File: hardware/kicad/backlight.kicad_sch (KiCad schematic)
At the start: 6 parts, among them J701 Retroilluminazione display, J702 USB del Pico (TP2/TP3), J703 USB del Pi Zero 2 W, U701 TPS61169 (Adafruit 6354)

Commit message: Translate code, hardware and docs to English; bilingual dashboard
- tdm-logic i18n module: every dashboard text in English and Italian,
  chosen by `[display] language` in the profile (English by default, the
  TDM 850 profile keeps Italian); number formatting per language
- Slint fixed labels moved to a `Labels` global filled from the same table;
  `tdm-dash --language en|it`; reference screens regenerated in English with
  Italian check screens
- tdmctl, tdm-dash CLI, simulator scenarios, calibration errors and tools
  print English
- KiCad sheets, WireViz harnesses, perfboard plan and CAD comments in
  English, exports regenerated with the new names
- manual, research, ADRs and READMEs translated; files renamed (docs/manual,
  docs/research, English chapter and ADR names); status markers are now
  [VERIFIED] / [TO VERIFY] / [HYPOTHESIS]

Co-Authored-By: Claude Opus 5.5 <noreply@anthropic.com>
Claude-Session: https://claude.ai/code/session_01G9D4Wshjz9MkaThp4wsrGP
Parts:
- J701: value Retroilluminazione display -> Display backlight
- J702: value USB del Pico (TP2/TP3) -> Pico USB (TP2/TP3)
- J703: value USB del Pi Zero 2 W -> Pi Zero 2 W USB
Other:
- note added: "1 VBUS (not connected) · 2 D− · 3 D+ · 4 GND Short twisted pair, ferrite on the cable."
- note added: "Backlight and USB to the Pi"
- note added: "The Pico drives the TPS61169 with 25 kHz PWM (GP15). 100 kΩ to ground: until the firmware runs, the backlight stays off (fail-dark). Newhaven display: LED 180 mA at 9.3 V. Module and display pins [TO VERIFY]. USB: only D+, D− and ground. VBUS not connected: the Pico is supplied from VSYS."
- note added: "The display connects to the Pi through the Adafruit DPI Kippah (40-pin FFC connector, off this board)."
- note removed: "1 VBUS (non collegato) · 2 D− · 3 D+ · 4 GND Doppino intrecciato corto, ferrite sul cavo."
- note removed: "Il Pico comanda il TPS61169 in PWM a 25 kHz (GP15). 100 kΩ verso massa: finché il firmware non parte la retroilluminazione resta spenta (fail-dark). Display Newhaven: LED 180 mA a 9,3 V. Pin del modulo e del display [DA VERIFICARE]. USB: solo D+, D− e massa. VBUS non collegato: il Pico si alimenta da VSYS."
- note removed: "Il display si collega al Pi con l'Adafruit DPI Kippah (connettore FFC 40 poli, fuori da questa scheda)."
- note removed: "Retroilluminazione e USB verso il Pi"
- title: Retroilluminazione e collegamento al Pi -> Backlight and link to the Pi
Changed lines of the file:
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@@
 	(paper "A4")
 	(title_block
-		(title "Retroilluminazione e collegamento al Pi")
+		(title "Backlight and link to the Pi")
 		(date "2026-10-21")
 		(rev "0.1")
 		(company "tdm-dash · CERN-OHL-P-2.0")
-		(comment 1 "Foglio 7 di 8")
-		(comment 2 "Generato da hardware/kicad/generate.py: non modificare a mano")
+		(comment 1 "Sheet 7 of 8")
+		(comment 2 "Generated by hardware/kicad/generate.py: do not edit by hand")
 	)
 	(symbol
@@
 			)
 		)
-		(property "Value" "Retroilluminazione display"
+		(property "Value" "Display backlight"
 			(at 155.194 68.58 0)
 			(effects
@@
 			)
 		)
-		(property "Value" "USB del Pico (TP2/TP3)"
+		(property "Value" "Pico USB (TP2/TP3)"
 			(at 50.8 134.62 0)
 			(effects
@@
 			)
 		)
-		(property "Value" "USB del Pi Zero 2 W"
+		(property "Value" "Pi Zero 2 W USB"
 			(at 139.7 134.62 0)
 			(effects
@@
 		)
 	)
-	(text "Retroilluminazione e USB verso il Pi"
+	(text "Backlight and USB to the Pi"
 		(exclude_from_sim no)
 		(at 10.16 12.7 0)
@@
 		)
 	)
-	(text "Il Pico comanda il TPS61169 in PWM a 25 kHz (GP15). 100 kΩ verso massa: finché il\nfirmware non parte la retroilluminazione resta spenta (fail-dark).\nDisplay Newhaven: LED 180 mA a 9,3 V. Pin del modulo e del display [DA VERIFICARE].\nUSB: solo D+, D− e massa. VBUS non collegato: il Pico si alimenta da VSYS."
+	(text "The Pico drives the TPS61169 with 25 kHz PWM (GP15). 100 kΩ to ground: until the\nfirmware runs, the backlight stays off (fail-dark).\nNewhaven display: LED 180 mA at 9.3 V. Module and display pins [TO VERIFY].\nUSB: only D+, D− and ground. VBUS not connected: the Pico is supplied from VSYS."
 		(exclude_from_sim no)
 		(at 10.16 17.78 0)
@@
 		)
 	)
-	(text "1 VBUS (non collegato) · 2 D− · 3 D+ · 4 GND\nDoppino intrecciato corto, ferrite sul cavo."
+	(text "1 VBUS (not connected) · 2 D− · 3 D+ · 4 GND\nShort twisted pair, ferrite on the cable."
 		(exclude_from_sim no)
 		(at 30.48 147.32 0)
@@
 		)
 	)
-	(text "Il display si collega al Pi con l'Adafruit DPI Kippah\n(connettore FFC 40 poli, fuori da questa scheda)."
+	(text "The display connects to the Pi through the Adafruit DPI Kippah\n(40-pin FFC connector, off this board)."
 		(exclude_from_sim no)
 		(at 190.5 121.92 0)

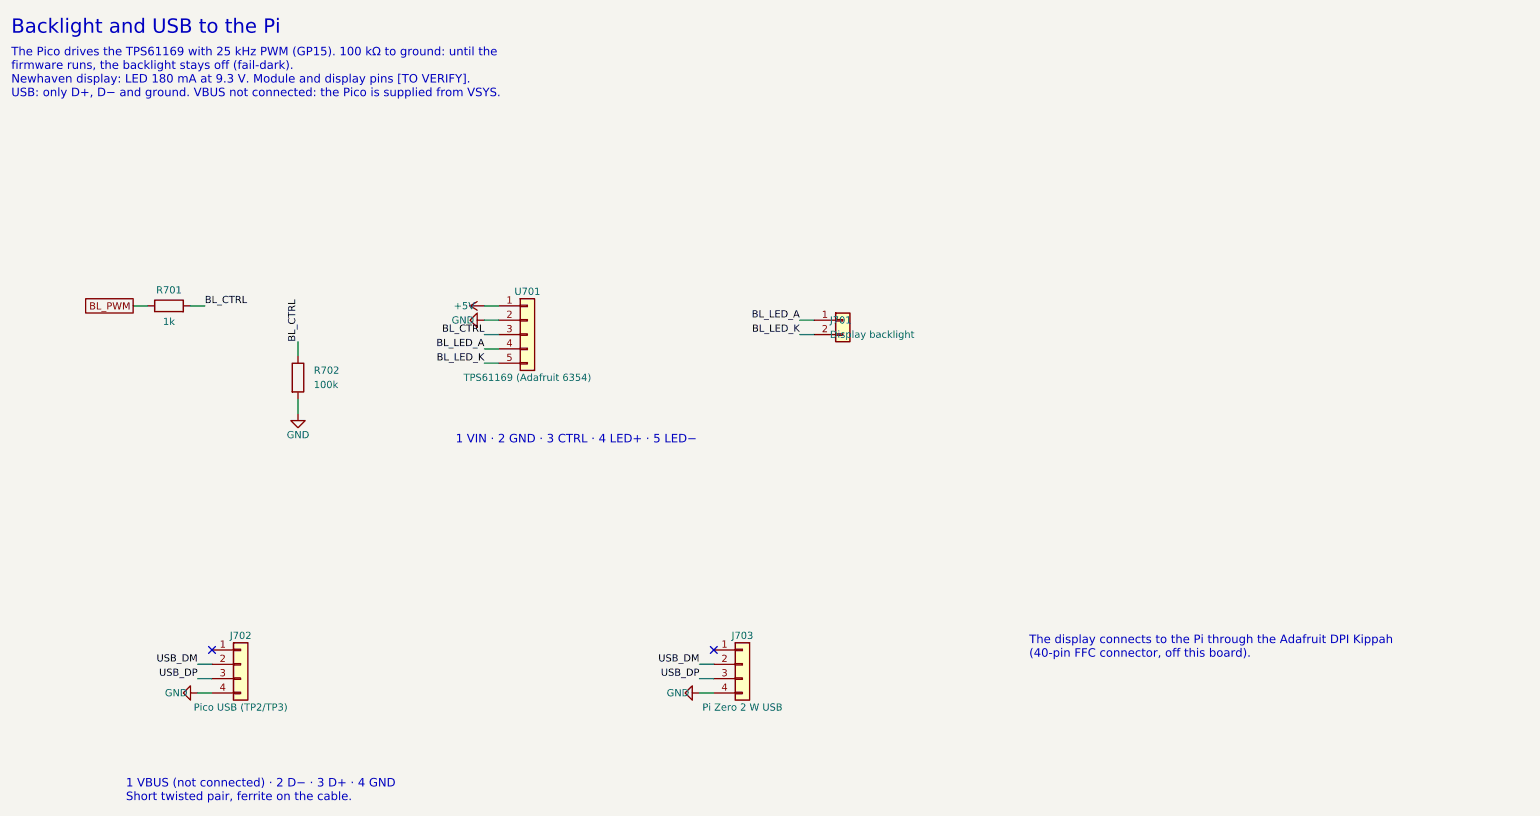
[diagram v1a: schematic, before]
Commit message: Schematic: drawn wires, block diagram, new title block
The sheets were a netlist in disguise: every pin ended in a short stub and
a label, so the circuits had to be pieced together by name, labels
overlapped, two sheets fell off the index page and the title block was
KiCad's default. The generator now draws the schematic:

- hardware/kicad/schgen: placement on the 50 mil grid, orthogonal wires,
  junctions, hierarchical ports, module and connector symbols with named
  pins; the drawing is normalised the way KiCad 9 reads it and checked
  against the declared netlist (no wire may connect anything else)
- hardware/kicad/sheets: one module per sheet, laid out left to right
  from the bike to the Pico; the root sheet is a block diagram whose
  wires are the signals between sheets
- tdm-dash.kicad_wks: frame and title block of the project
- symbols copied from KiCad 9.0.9 (vendor_symbols.py): the generator no
  longer needs KiCad installed
- export.sh: ERC, tools/check_netlist.py (KiCad's netlist is the declared
  one), check_pinmap.py, PDF and SVG on white, tools/check_svg_layout.py
  (no text over another text, a wire, the frame or the title block)

The circuit is unchanged: KiCad's netlist of the old and new schematic
has the same 56 nets (FRAM pins now follow the breakout header, R603/R604
pins swapped).

Co-Authored-By: Claude Opus 5.5 <noreply@anthropic.com>
Claude-Session: https://claude.ai/code/session_01G9D4Wshjz9MkaThp4wsrGP
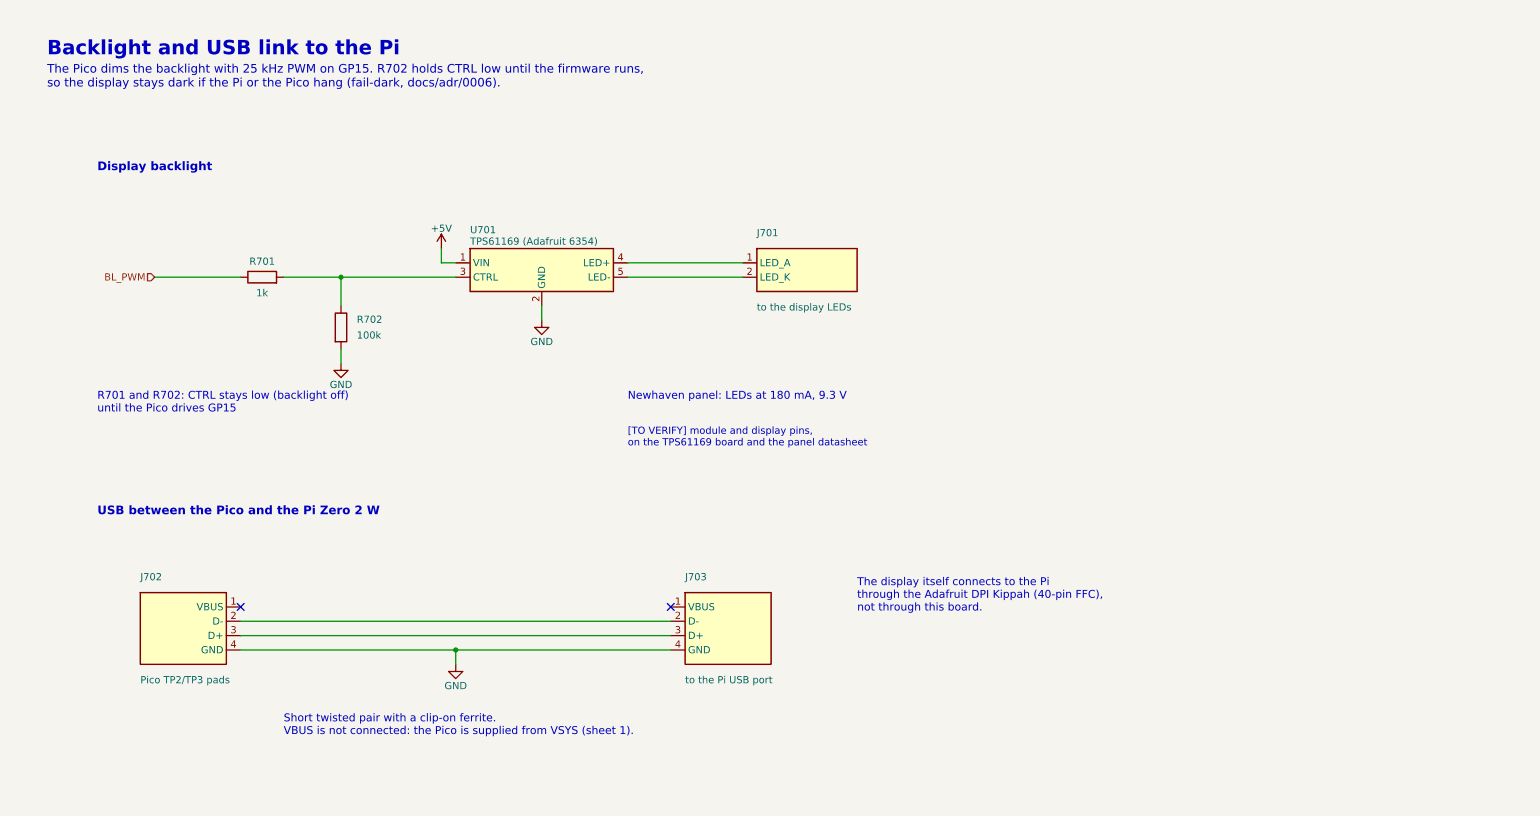
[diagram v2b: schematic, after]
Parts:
- removed J701: Display backlight, symbol Connector_Generic:Conn_01x02
- removed J702: Pico USB (TP2/TP3), symbol Connector_Generic:Conn_01x04
- removed J703: Pi Zero 2 W USB, symbol Connector_Generic:Conn_01x04
- removed U701: TPS61169 (Adafruit 6354), symbol Connector_Generic:Conn_01x05
- added J701: to the display LEDs, symbol tdm:Conn_Backlight2
- added J702: Pico TP2/TP3 pads, symbol tdm:Conn_USB_Pico
- added J703: to the Pi USB port, symbol tdm:Conn_USB_Pi
- added U701: TPS61169 (Adafruit 6354), symbol tdm:TPS61169_Module
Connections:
- net +5V: now also U701.1 (VIN)
- net GND: now also J702.4 (GND), J703.4 (GND), U701.2 (GND)
- net BL_CTRL: no longer names the net of R701.2, R702.1
- net BL_CTRL: now also U701.3 (CTRL)
- new net: J701.1 (LED_A), U701.4 (LED+)
- new net: J701.2 (LED_K), U701.5 (LED-)
- new net: J702.2 (D-), J703.2 (D-)
- new net: J702.3 (D+), J703.3 (D+)
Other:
- note added: "Backlight and USB link to the Pi"
- note added: "Display backlight"
- note added: "Newhaven panel: LEDs at 180 mA, 9.3 V"
- note added: "R701 and R702: CTRL stays low (backlight off) until the Pico drives GP15"
- note added: "Short twisted pair with a clip-on ferrite. VBUS is not connected: the Pico is supplied from VSYS (sheet 1)."
- note added: "The Pico dims the backlight with 25 kHz PWM on GP15. R702 holds CTRL low until the firmware runs, so the display stays dark if the Pi or the Pico hang (fail-dark, docs/adr/0006)."
- note added: "The display itself connects to the Pi through the Adafruit DPI Kippah (40-pin FFC), not through this board."
- note added: "USB between the Pico and the Pi Zero 2 W"
- note added: "[TO VERIFY] module and display pins, on the TPS61169 board and the panel datasheet"
- note removed: "1 VBUS (not connected) · 2 D− · 3 D+ · 4 GND Short twisted pair, ferrite on the cable."
- note removed: "1 VIN · 2 GND · 3 CTRL · 4 LED+ · 5 LED−"
- note removed: "Backlight and USB to the Pi"
- note removed: "The Pico drives the TPS61169 with 25 kHz PWM (GP15). 100 kΩ to ground: until the firmware runs, the backlight stays off (fail-dark). Newhaven display: LED 180 mA at 9.3 V. Module and display pins [TO VERIFY]. USB: only D+, D− and ground. VBUS not connected: the Pico is supplied from VSYS."
- note removed: "The display connects to the Pi through the Adafruit DPI Kippah (40-pin FFC connector, off this board)."
- company: tdm-dash · CERN-OHL-P-2.0 -> tdm-dash

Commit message: Schematic: backlight breakout off the board, harness fuse, micro-USB plug
The perfboard has no room for the TPS61169 breakout, and the build steps
already wired it off the board: J701 now gives it +5 V, CTRL and ground,
and its output goes to the panel LED pins (J704), in a dashed box like the
buttons. F101 is marked as the inline fuse of the adapter harness, J401 as
the terminal for the sensor cable, and J703 has the five pins of the
micro-USB plug, with ID tied to ground.

Co-Authored-By: Claude Opus 5.5 <noreply@anthropic.com>
Claude-Session: https://claude.ai/code/session_01G9D4Wshjz9MkaThp4wsrGP
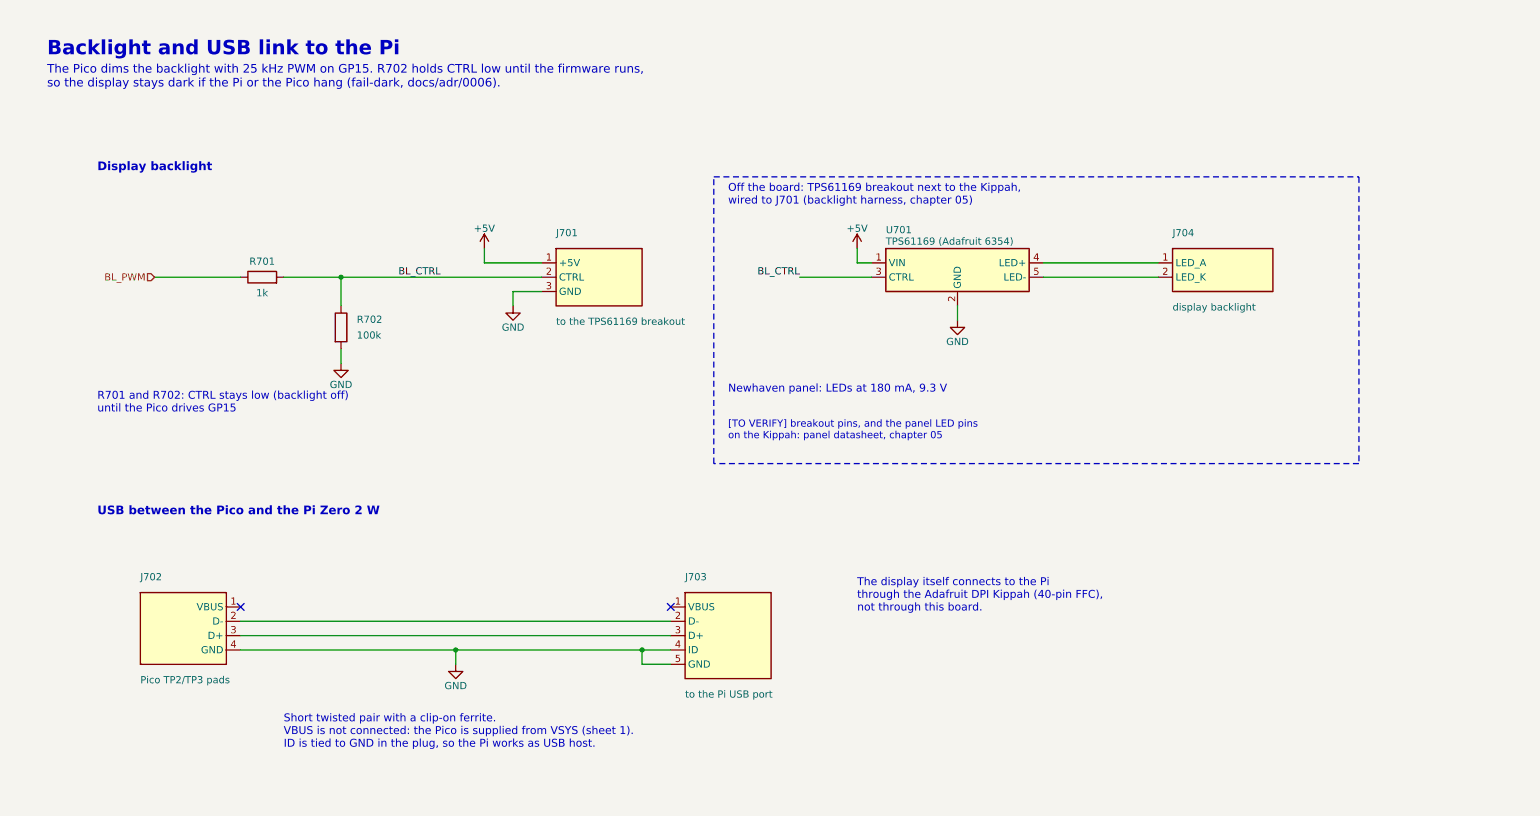
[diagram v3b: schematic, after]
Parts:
- added J704: display backlight, symbol tdm:Conn_Backlight2
- J701: value to the display LEDs -> to the TPS61169 breakout; symbol tdm:Conn_Backlight2 -> tdm:Conn_BLDriver3
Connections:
- net +5V: now also J701.1 (+5V)
- net GND: now also J701.3 (GND), J703.5 (GND)
- net BL_CTRL: now reaches R701.2, R702.1, U701.3 (CTRL)
- net BL_CTRL: now also J701.2 (CTRL)
- net at U701.4 (LED+): now also J704.1 (LED_A); no longer J701.1 (LED_A)
- net at U701.5 (LED-): now also J704.2 (LED_K); no longer J701.2 (LED_K)
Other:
- note added: "Off the board: TPS61169 breakout next to the Kippah, wired to J701 (backlight harness, chapter 05)"
- note added: "Short twisted pair with a clip-on ferrite. VBUS is not connected: the Pico is supplied from VSYS (sheet 1). ID is tied to GND in the plug, so the Pi works as USB host."
- note added: "[TO VERIFY] breakout pins, and the panel LED pins on the Kippah: panel datasheet, chapter 05"
- note removed: "Short twisted pair with a clip-on ferrite. VBUS is not connected: the Pico is supplied from VSYS (sheet 1)."
- note removed: "[TO VERIFY] module and display pins, on the TPS61169 board and the panel datasheet"
- moved on the sheet: U701
